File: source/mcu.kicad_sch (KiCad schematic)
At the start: 34 parts, among them J5 Conn_01x04_Male, J6 TYPE-C-31-M-12, U14 TJA1050T/CM,118, U15 STM32F405RGT6, Y1 8MHz Crystal Resonator, X5032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

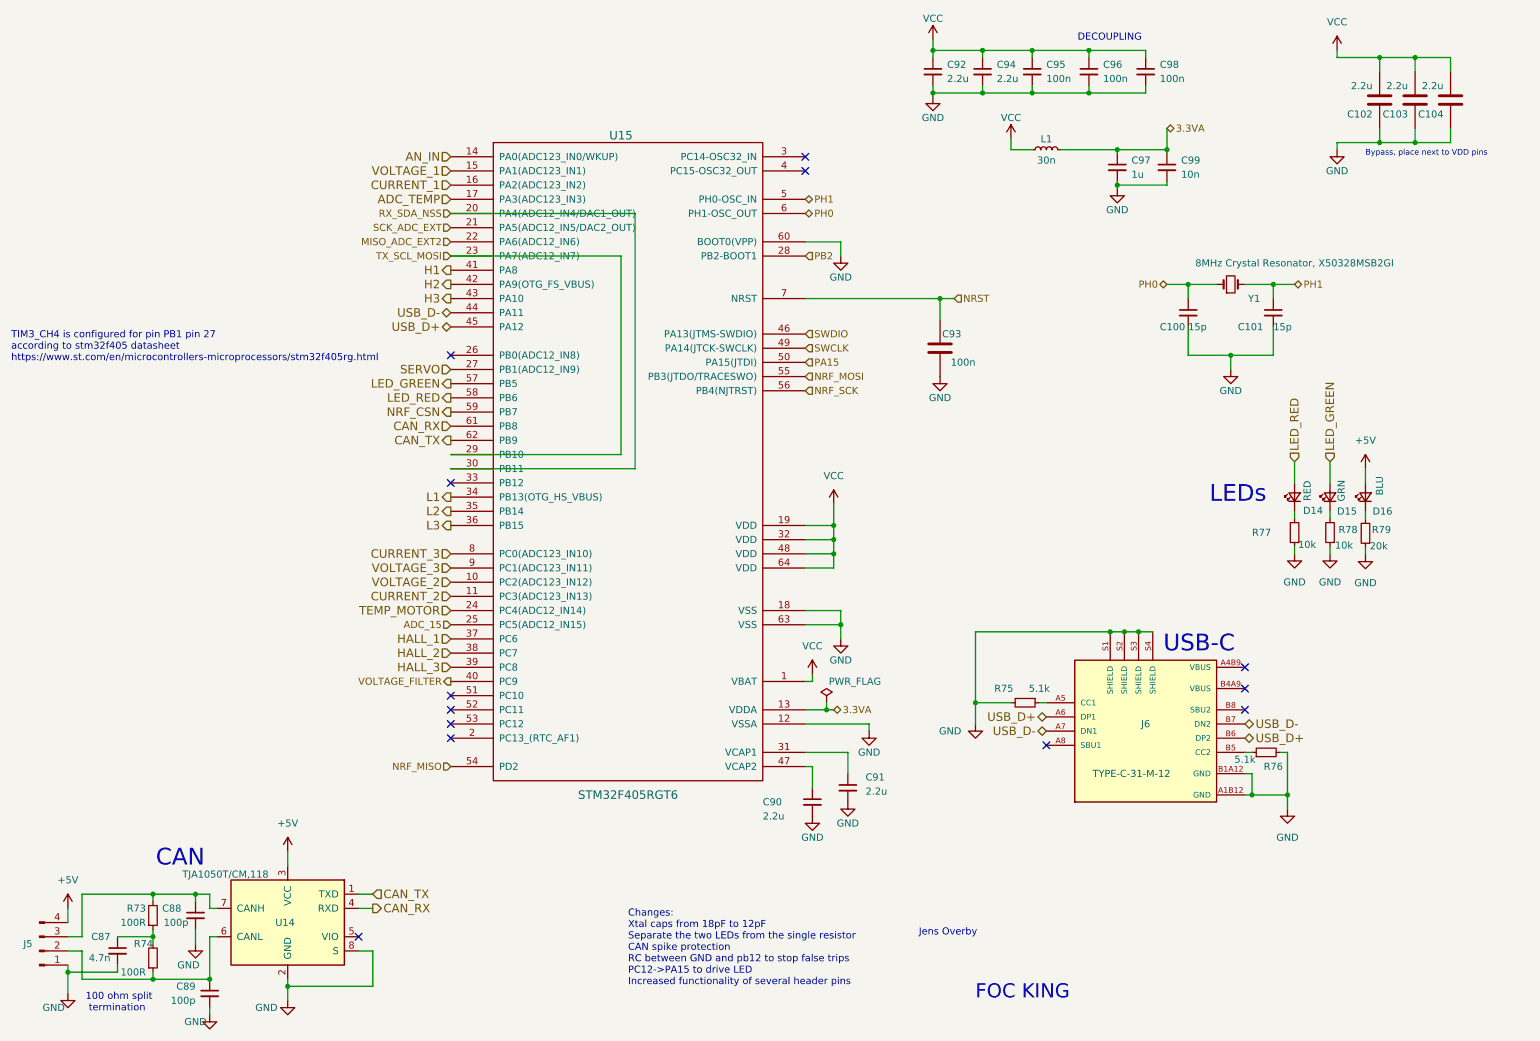
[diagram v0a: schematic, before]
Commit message: 4 layer design
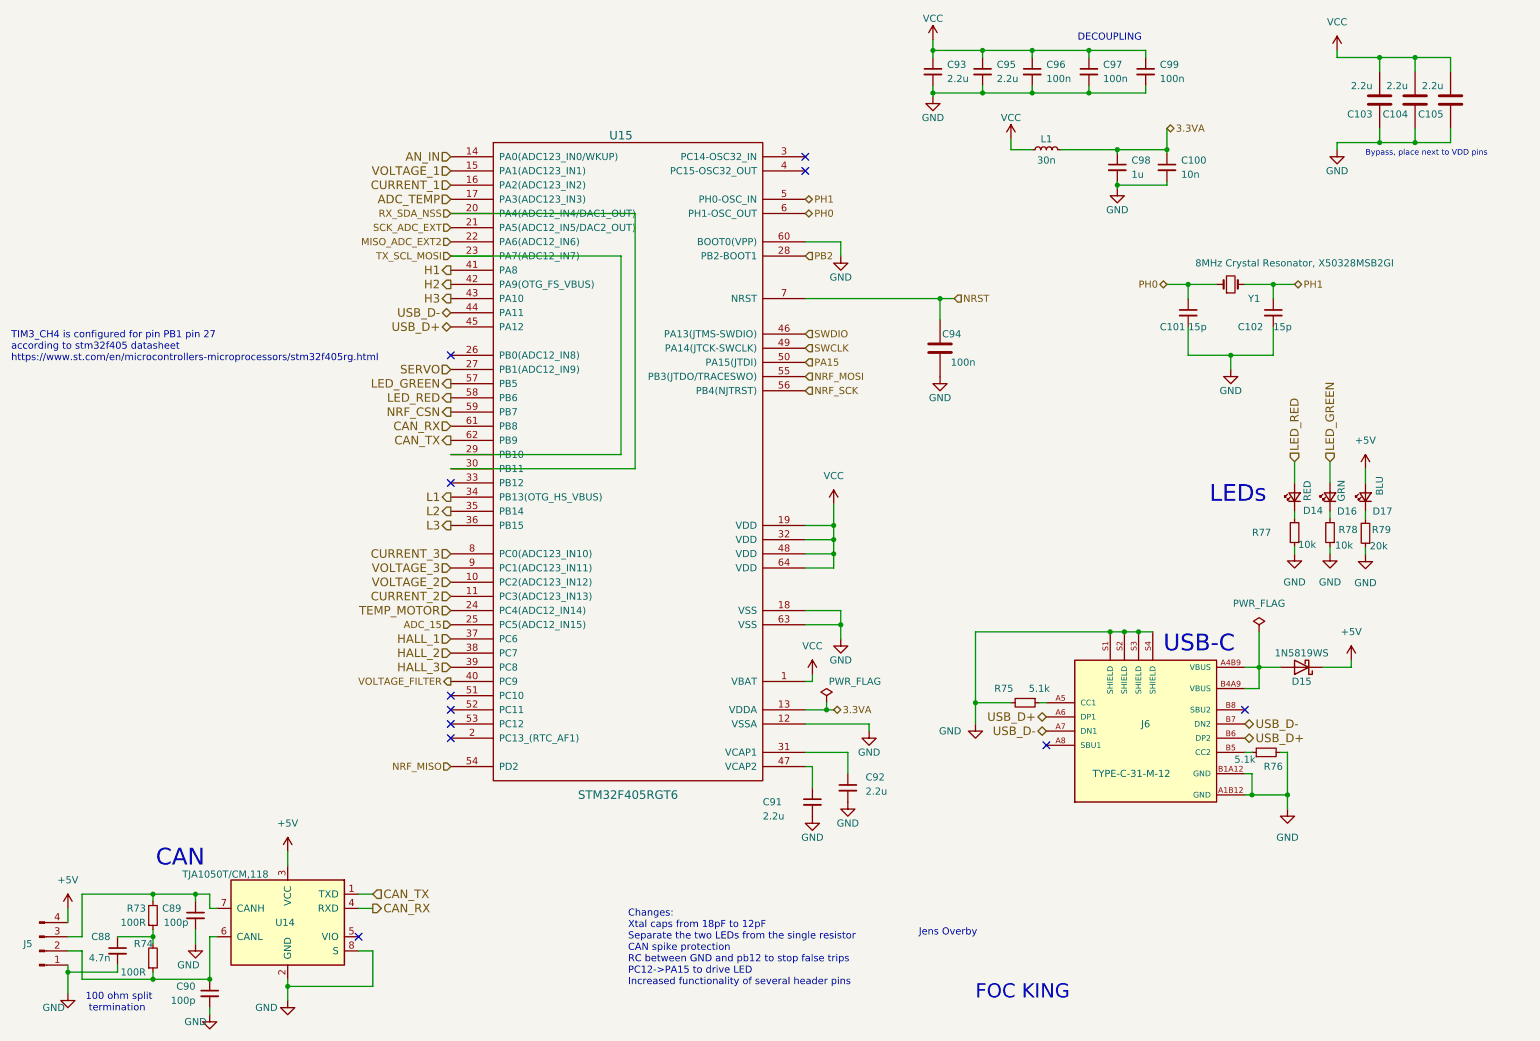
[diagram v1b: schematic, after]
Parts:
- added D15: 1N5819WS, Diode_SMD:D_SOD-323, symbol Device:D_Schottky
- renumbered C99 to C100, C100 to C101, C101 to C102, C102 to C103, C103 to C104, C104 to C105, C87 to C88, C88 to C89, C89 to C90, C90 to C91, C91 to C92, C92 to C93, C93 to C94, C94 to C95, C95 to C96, C96 to C97, C97 to C98, C98 to C99, D15 to D16, D16 to D17
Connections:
- net +5V: now also D15.1 (K)
- net at J6.A4B9 (VBUS): now also J6.B4A9 (VBUS), D15.2 (A)
- no-connect marks 13 -> 11

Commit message: First 4 layer order at JLCPCB
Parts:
- renumbered J5 to J4, J6 to J5
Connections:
- net CURRENT_3: now also U15.9 (PC1(ADC123_IN11)); no longer U15.8 (PC0(ADC123_IN10))
- net RX_SDA_NSS: no longer U15.30 (PB11)
- net TX_SCL_MOSI: no longer U15.29 (PB10)
- net VOLTAGE_3: now also U15.8 (PC0(ADC123_IN10)); no longer U15.9 (PC1(ADC123_IN11))
- net NRF_CSN: no longer names the net of U15.59 (PB7)
- net NRF_MISO: no longer names the net of U15.54 (PD2)
- net NRF_MOSI: no longer names the net of U15.55 (PB3(JTDO/TRACESWO))
- net NRF_SCK: no longer names the net of U15.56 (PB4(NJTRST))
- no-connect marks 11 -> 17

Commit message: Add files via upload
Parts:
- renumbered C88 to C82, C89 to C83, C90 to C84, C91 to C85, C92 to C86, C93 to C87, C94 to C88, C95 to C89, C96 to C90, C97 to C91, C98 to C92, C99 to C93, C100 to C94, C101 to C95, C102 to C96, C103 to C97, C104 to C98, C105 to C99, R73 to R67, R74 to R68, R75 to R69, R76 to R70, R77 to R71, R78 to R72, R79 to R73
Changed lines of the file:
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@@
   (symbol (lib_id "Device:C_Small") (at 218.44 25.4 0) (unit 1)
     (in_bom yes) (on_board yes)
-    (property "Reference" "C99" (id 0) (at 220.98 24.13 0)
+    (property "Reference" "C93" (id 0) (at 220.98 24.13 0)
       (effects (font (size 1.27 1.27)) (justify left))
     )
@@
   (symbol (lib_id "Device:R_Small") (at 40.64 176.53 0) (mirror x) (unit 1)
     (in_bom yes) (on_board yes)
-    (property "Reference" "R73" (id 0) (at 39.37 175.26 0)
+    (property "Reference" "R67" (id 0) (at 39.37 175.26 0)
       (effects (font (size 1.27 1.27)) (justify right))
     )
@@
   (symbol (lib_id "Device:R_Small") (at 245.11 107.95 180) (unit 1)
     (in_bom yes) (on_board yes)
-    (property "Reference" "R77" (id 0) (at 237.49 107.95 0)
+    (property "Reference" "R71" (id 0) (at 237.49 107.95 0)
       (effects (font (size 1.27 1.27)) (justify right))
     )
@@
   (symbol (lib_id "Device:C_Small") (at 48.26 176.53 0) (mirror y) (unit 1)
     (in_bom yes) (on_board yes)
-    (property "Reference" "C89" (id 0) (at 45.72 175.26 0)
+    (property "Reference" "C83" (id 0) (at 45.72 175.26 0)
       (effects (font (size 1.27 1.27)) (justify left))
     )
@@
   (symbol (lib_id "BLDC_4-rescue:C-RESCUE-BLDC_4") (at 273.05 30.48 180) (unit 1)
     (in_bom yes) (on_board yes)
-    (property "Reference" "C105" (id 0) (at 271.78 33.02 0)
+    (property "Reference" "C99" (id 0) (at 271.78 33.02 0)
       (effects (font (size 1.27 1.27)) (justify left))
     )
@@
   (symbol (lib_id "Device:C_Small") (at 198.12 25.4 0) (unit 1)
     (in_bom yes) (on_board yes)
-    (property "Reference" "C96" (id 0) (at 200.66 24.13 0)
+    (property "Reference" "C90" (id 0) (at 200.66 24.13 0)
       (effects (font (size 1.27 1.27)) (justify left))
     )
@@
   (symbol (lib_id "Device:R_Small") (at 196.85 138.43 270) (unit 1)
     (in_bom yes) (on_board yes)
-    (property "Reference" "R75" (id 0) (at 193.04 135.89 90))
+    (property "Reference" "R69" (id 0) (at 193.04 135.89 90))
     (property "Value" "5.1k" (id 1) (at 199.39 135.89 90))
     (property "Footprint" "Resistor_SMD:R_0603_1608Metric" (id 2) (at 196.85 138.43 0)
@@
   (symbol (lib_id "BLDC_4-rescue:C-RESCUE-BLDC_4") (at 266.7 30.48 180) (unit 1)
     (in_bom yes) (on_board yes)
-    (property "Reference" "C104" (id 0) (at 265.43 33.02 0)
+    (property "Reference" "C98" (id 0) (at 265.43 33.02 0)
       (effects (font (size 1.27 1.27)) (justify left))
     )
@@
   (symbol (lib_id "Device:C_Small") (at 189.23 25.4 0) (unit 1)
     (in_bom yes) (on_board yes)
-    (property "Reference" "C95" (id 0) (at 191.77 24.13 0)
+    (property "Reference" "C89" (id 0) (at 191.77 24.13 0)
       (effects (font (size 1.27 1.27)) (justify left))
     )
@@
   (symbol (lib_id "Device:C_Small") (at 208.28 25.4 0) (unit 1)
     (in_bom yes) (on_board yes)
-    (property "Reference" "C97" (id 0) (at 210.82 24.13 0)
+    (property "Reference" "C91" (id 0) (at 210.82 24.13 0)
       (effects (font (size 1.27 1.27)) (justify left))
     )
@@
   (symbol (lib_id "Device:R_Small") (at 251.46 107.95 180) (unit 1)
     (in_bom yes) (on_board yes)
-    (property "Reference" "R78" (id 0) (at 252.984 107.442 0)
+    (property "Reference" "R72" (id 0) (at 252.984 107.442 0)
       (effects (font (size 1.27 1.27)) (justify right))
     )
@@
   (symbol (lib_id "Device:R_Small") (at 40.64 184.15 0) (mirror x) (unit 1)
     (in_bom yes) (on_board yes)
-    (property "Reference" "R74" (id 0) (at 40.64 181.61 0)
+    (property "Reference" "R68" (id 0) (at 40.64 181.61 0)
       (effects (font (size 1.27 1.27)) (justify right))
     )
@@
   (symbol (lib_id "Device:C_Small") (at 158.75 156.21 0) (unit 1)
     (in_bom yes) (on_board yes)
-    (property "Reference" "C91" (id 0) (at 149.86 156.21 0)
+    (property "Reference" "C85" (id 0) (at 149.86 156.21 0)
       (effects (font (size 1.27 1.27)) (justify left))
     )
@@
   (symbol (lib_id "Device:C_Small") (at 165.1 153.67 0) (unit 1)
     (in_bom yes) (on_board yes)
-    (property "Reference" "C92" (id 0) (at 168.275 151.765 0)
+    (property "Reference" "C86" (id 0) (at 168.275 151.765 0)
       (effects (font (size 1.27 1.27)) (justify left))
     )
@@
   (symbol (lib_id "Device:C_Small") (at 50.8 190.5 0) (mirror y) (unit 1)
     (in_bom yes) (on_board yes)
-    (property "Reference" "C90" (id 0) (at 48.26 189.23 0)
+    (property "Reference" "C84" (id 0) (at 48.26 189.23 0)
       (effects (font (size 1.27 1.27)) (justify left))
     )
@@
   (symbol (lib_id "BLDC_4-rescue:C-RESCUE-BLDC_4") (at 260.35 30.48 180) (unit 1)
     (in_bom yes) (on_board yes)
-    (property "Reference" "C103" (id 0) (at 259.08 33.02 0)
+    (property "Reference" "C97" (id 0) (at 259.08 33.02 0)
       (effects (font (size 1.27 1.27)) (justify left))
     )
@@
   (symbol (lib_id "Device:C_Small") (at 213.36 42.545 0) (unit 1)
     (in_bom yes) (on_board yes)
-    (property "Reference" "C98" (id 0) (at 215.9 41.275 0)
+    (property "Reference" "C92" (id 0) (at 215.9 41.275 0)
       (effects (font (size 1.27 1.27)) (justify left))
     )
@@
   (symbol (lib_id "Device:C_Small") (at 180.34 25.4 0) (unit 1)
     (in_bom yes) (on_board yes)
-    (property "Reference" "C93" (id 0) (at 182.88 24.13 0)
+    (property "Reference" "C87" (id 0) (at 182.88 24.13 0)
       (effects (font (size 1.27 1.27)) (justify left))
     )
@@
   (symbol (lib_id "Device:C_Small") (at 34.29 182.88 0) (mirror y) (unit 1)
     (in_bom yes) (on_board yes)
-    (property "Reference" "C88" (id 0) (at 33.02 180.34 0)
+    (property "Reference" "C82" (id 0) (at 33.02 180.34 0)
       (effects (font (size 1.27 1.27)) (justify left))
     )
@@
   (symbol (lib_id "Device:R_Small") (at 240.03 147.32 90) (unit 1)
     (in_bom yes) (on_board yes)
-    (property "Reference" "R76" (id 0) (at 241.3 149.86 90))
+    (property "Reference" "R70" (id 0) (at 241.3 149.86 90))
     (property "Value" "5.1k" (id 1) (at 236.22 148.59 90))
     (property "Footprint" "Resistor_SMD:R_0603_1608Metric" (id 2) (at 240.03 147.32 0)
@@
   (symbol (lib_id "BLDC_4-rescue:C-RESCUE-BLDC_4") (at 181.61 74.93 180) (unit 1)
     (in_bom yes) (on_board yes)
-    (property "Reference" "C94" (id 0) (at 185.42 72.39 0)
+    (property "Reference" "C88" (id 0) (at 185.42 72.39 0)
       (effects (font (size 1.27 1.27)) (justify left))
     )
@@
   (symbol (lib_id "Device:C_Small") (at 241.3 68.58 0) (unit 1)
     (in_bom yes) (on_board yes)
-    (property "Reference" "C102" (id 0) (at 234.95 71.12 0)
+    (property "Reference" "C96" (id 0) (at 234.95 71.12 0)
       (effects (font (size 1.27 1.27)) (justify left))
     )
@@
   (symbol (lib_id "Device:R_Small") (at 257.81 108.077 180) (unit 1)
     (in_bom yes) (on_board yes)
-    (property "Reference" "R79" (id 0) (at 258.953 107.442 0)
+    (property "Reference" "R73" (id 0) (at 258.953 107.442 0)
       (effects (font (size 1.27 1.27)) (justify right))
     )
@@
   (symbol (lib_id "Device:C_Small") (at 222.25 42.545 0) (unit 1)
     (in_bom yes) (on_board yes)
-    (property "Reference" "C100" (id 0) (at 224.79 41.275 0)
+    (property "Reference" "C94" (id 0) (at 224.79 41.275 0)
       (effects (font (size 1.27 1.27)) (justify left))
     )
@@
   (symbol (lib_id "Device:C_Small") (at 226.06 68.58 0) (unit 1)
     (in_bom yes) (on_board yes)
-    (property "Reference" "C101" (id 0) (at 220.98 71.12 0)
-      (effects (font (size 1.27 1.27)) (justify left))
-    )
+    (property "Reference" "C95" (id 0) (at 220.98 71.12 0)
+      (effects (font (size 1.27 1.27)) (justify left))
+    )
